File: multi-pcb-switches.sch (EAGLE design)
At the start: 39 parts, among them IC1 LM358N, K1 351, K2 RT184012, K3 RT184012, T1 BC618, T3 BC618, T4 BC618, X1 2.52B-ZR, X2 2.52B-ZR

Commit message: Routed more multi-pcb boards
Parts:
- removed APP, ECU: (no value), con-ptr500-custom:AK300/2
- removed C1, C2: 100u, rcl:C-EU025-050X050
- removed C4: 0.1u, rcl:C-EU025-050X050
- removed D1: 1N40047, diode-custom:1N40047
- removed D5, D6: BZX83C5V1, diode-custom:BZX857
- removed IC1: LM358N, linear:LM358N
- removed K1: 351, relay:351
- removed R1, R2: 150, rcl:R-EU_0309/10
- removed R10, R8: 10k, rcl:R-EU_0207/7
- removed R11, R9: 10k, rcl:R-EU_0309/10
- removed R12, R13: 1k, rcl:R-EU_0207/7
- removed R20, R3, R7: 2k, rcl:R-EU_0207/7
- removed R30, R31: >65, rcl:R-EU_0207/7
- removed T1: BC618, transistor-npn:BC618
- removed X1, X2: 2.52B-ZR, con-jst-custom:2.52B-ZR
- added X3: 2.55B-ZR, con-jst-custom:2.55B-ZR
- added X5: 2.52B-ZR, con-jst-custom:2.52B-ZR
- R32, R33: device rcl:R-EU_0309/10 -> rcl:R-EU_0207/7
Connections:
- removed net +5V: D1.C, K11.1
- removed net APP_0_IN: APP-2.KL, K13.O, R11.2, X1-1.1
- removed net APP_1_IN: APP-1.KL, K12.O, R9.2, X1-2.1
- removed net APP_ENABLE: R3.2
- removed net APP_PWM_OUT_0: R1.2
- removed net APP_PWM_OUT_1: R2.2
- removed net N$1: D1.A, K11.2, T1.C
- removed net N$13: IC1A.-IN, R12.2, R7.1
- removed net N$16: IC1B.-IN, R13.2, R20.1
- removed net N$17: D5.C, K13.S, R30.1
- removed net N$18: IC1B.OUT, R13.1, R31.2
- removed net N$2: R3.1, T1.B
- removed net N$3: D6.C, K12.S, R31.1
- removed net N$4: IC1A.OUT, R12.1, R30.2
- removed net N$6: ECU-2.KL, K13.P, X2-2.1
- removed net N$7: ECU-1.KL, K12.P, X2-1.1
- removed net N$8: C2.1, IC1A.+IN, R1.1
- removed net N$9: C1.1, IC1B.+IN, R2.1
- removed net SENS_APP_0_IN: R10.2, R11.1
- removed net SENS_APP_1_IN: R8.2, R9.1
- net +3V3: now also X3-5.1
- net BTN_0: now also X3-4.1
- net BTN_1: now also X3-3.1
- net CLAXON_ENABLE: now also X3-1.1
- net ENGINE_CUTOFF_DISABLE: now also X3-2.1
- net GND: now also X5-1.1; no longer C1.2, C2.2, C4.2, D5.A, D6.A, IC1P.V-, R10.1, R20.2, R7.2, R8.1, T1.E
- net PWR_IN+: now also X5-2.1; no longer C4.1, IC1P.V+
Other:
- note removed: "ACCELERATOR PEDAL SWITCH/DAC"
- note removed: "DAC circuit"
- note removed: "Gain 3.3V -> 5V"
- note removed: "Over voltage protection"
- note removed: "Source selection circuit"
- note removed: "Voltage divider (5v -> 2.5v)"

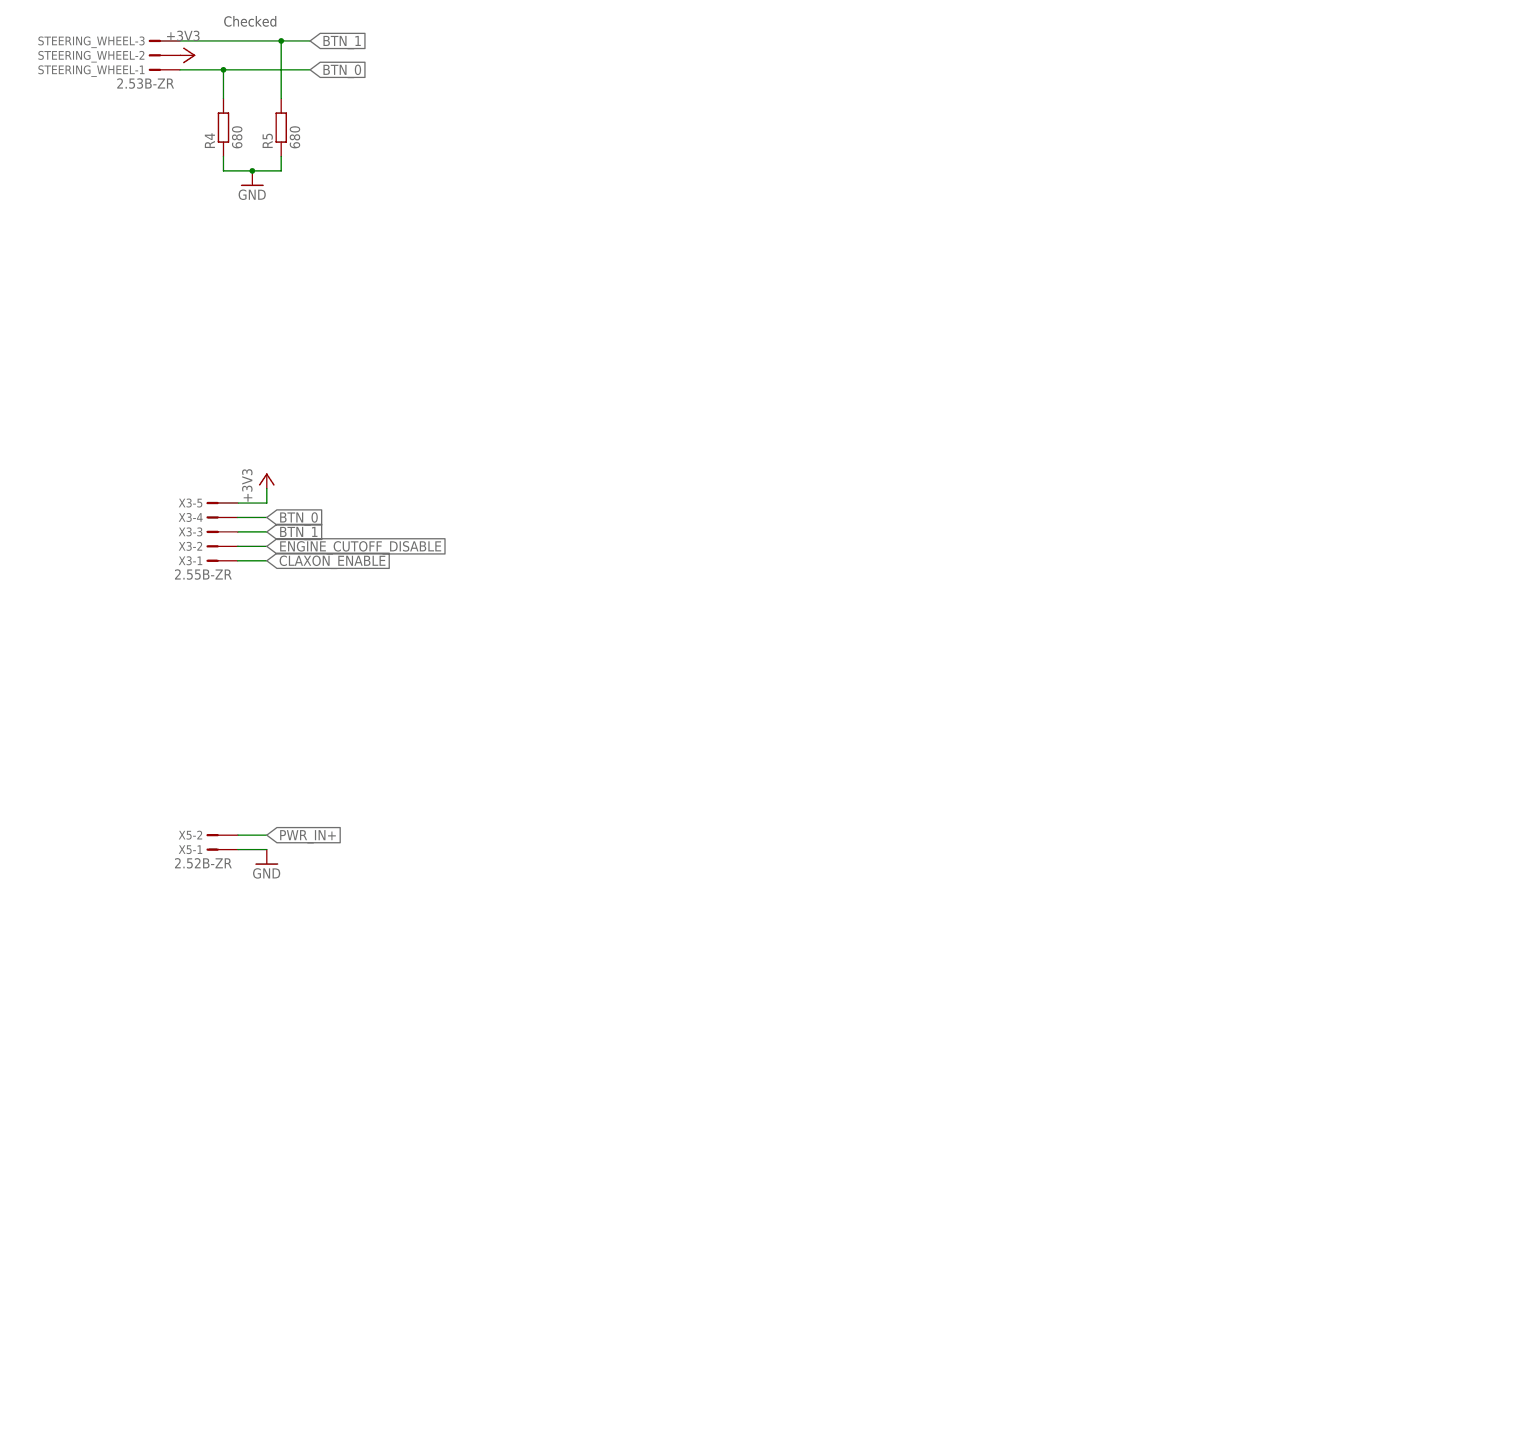
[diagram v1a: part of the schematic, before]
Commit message: Made schematic more compact/clean
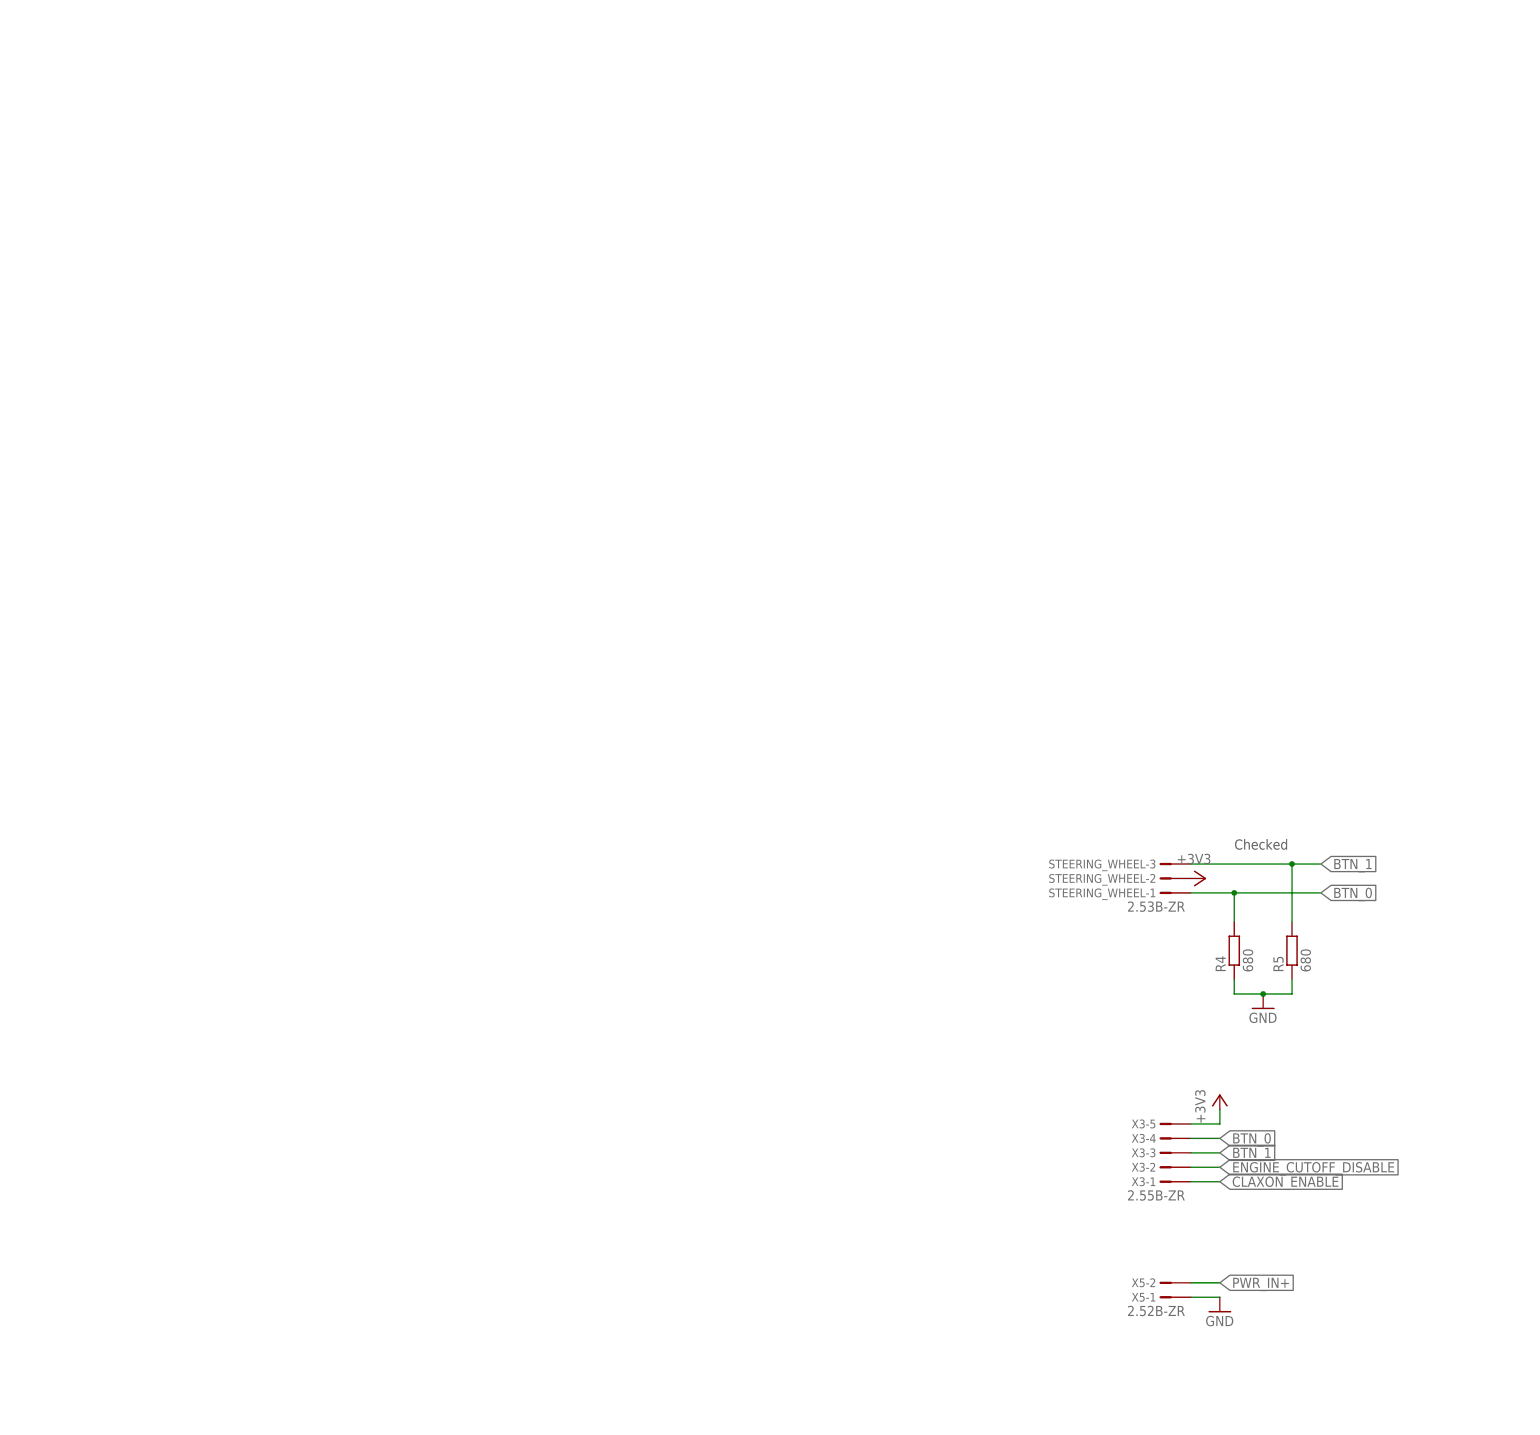
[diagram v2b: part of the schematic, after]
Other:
- moved on the sheet: R4, R5, STEERING_WHEEL-1, STEERING_WHEEL-2, STEERING_WHEEL-3, X3-1, X3-2, X3-3, X3-4, X3-5, X5-1, X5-2
